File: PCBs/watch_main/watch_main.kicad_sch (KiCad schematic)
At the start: 1 part, among them U101 Watch_Outline

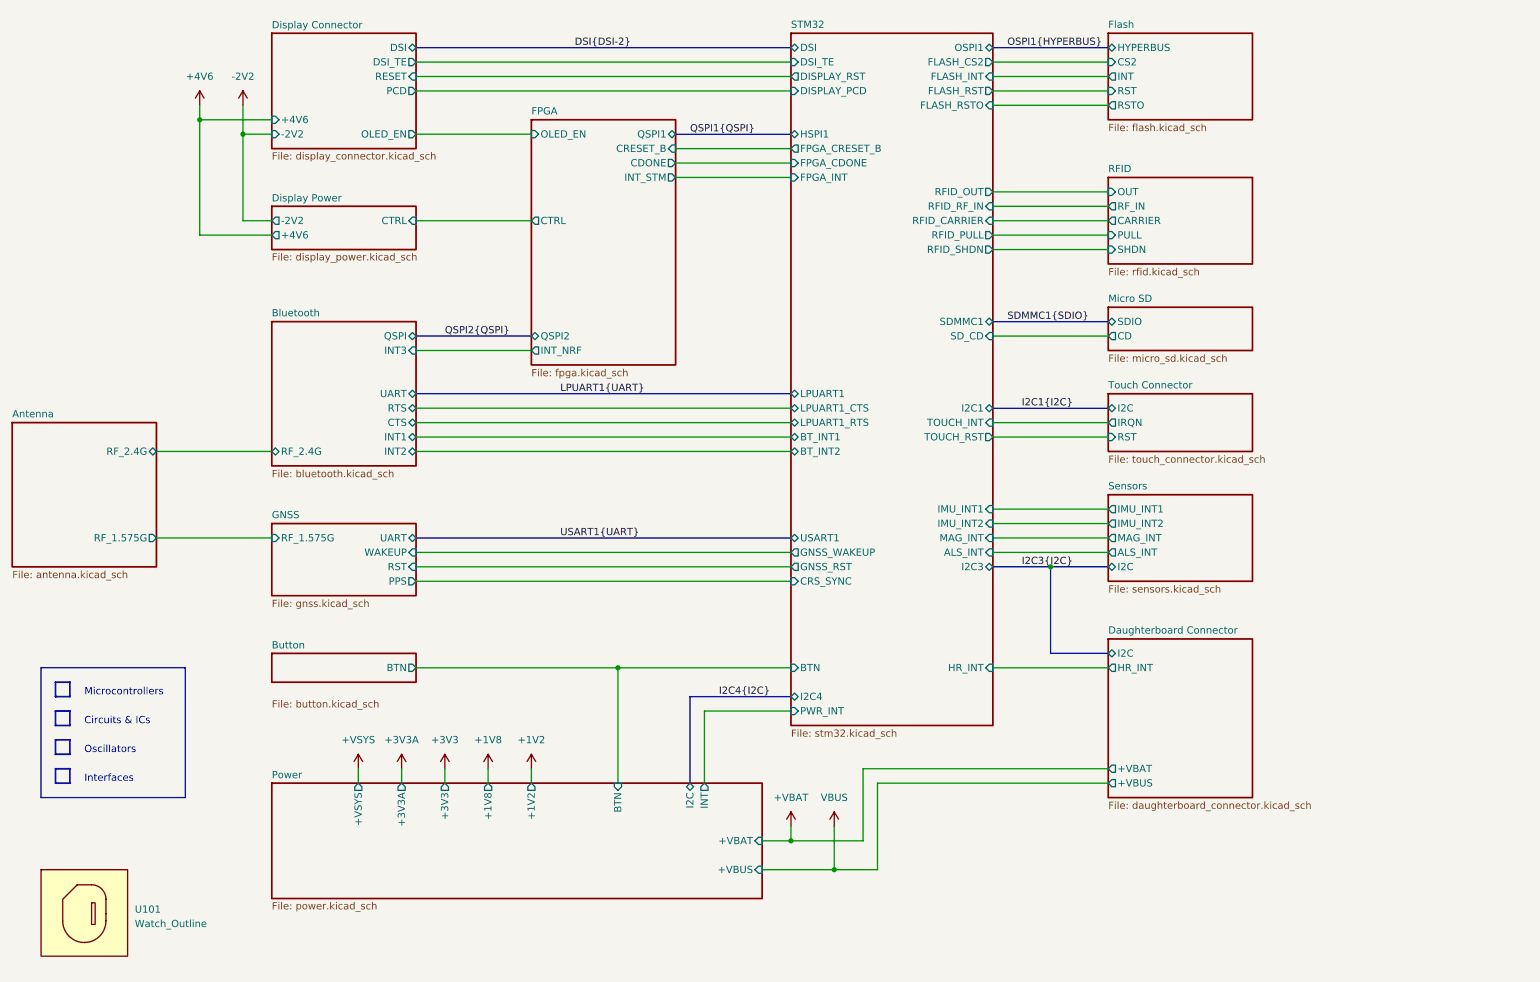
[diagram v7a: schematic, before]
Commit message: Progress with schematic and RFID simulations
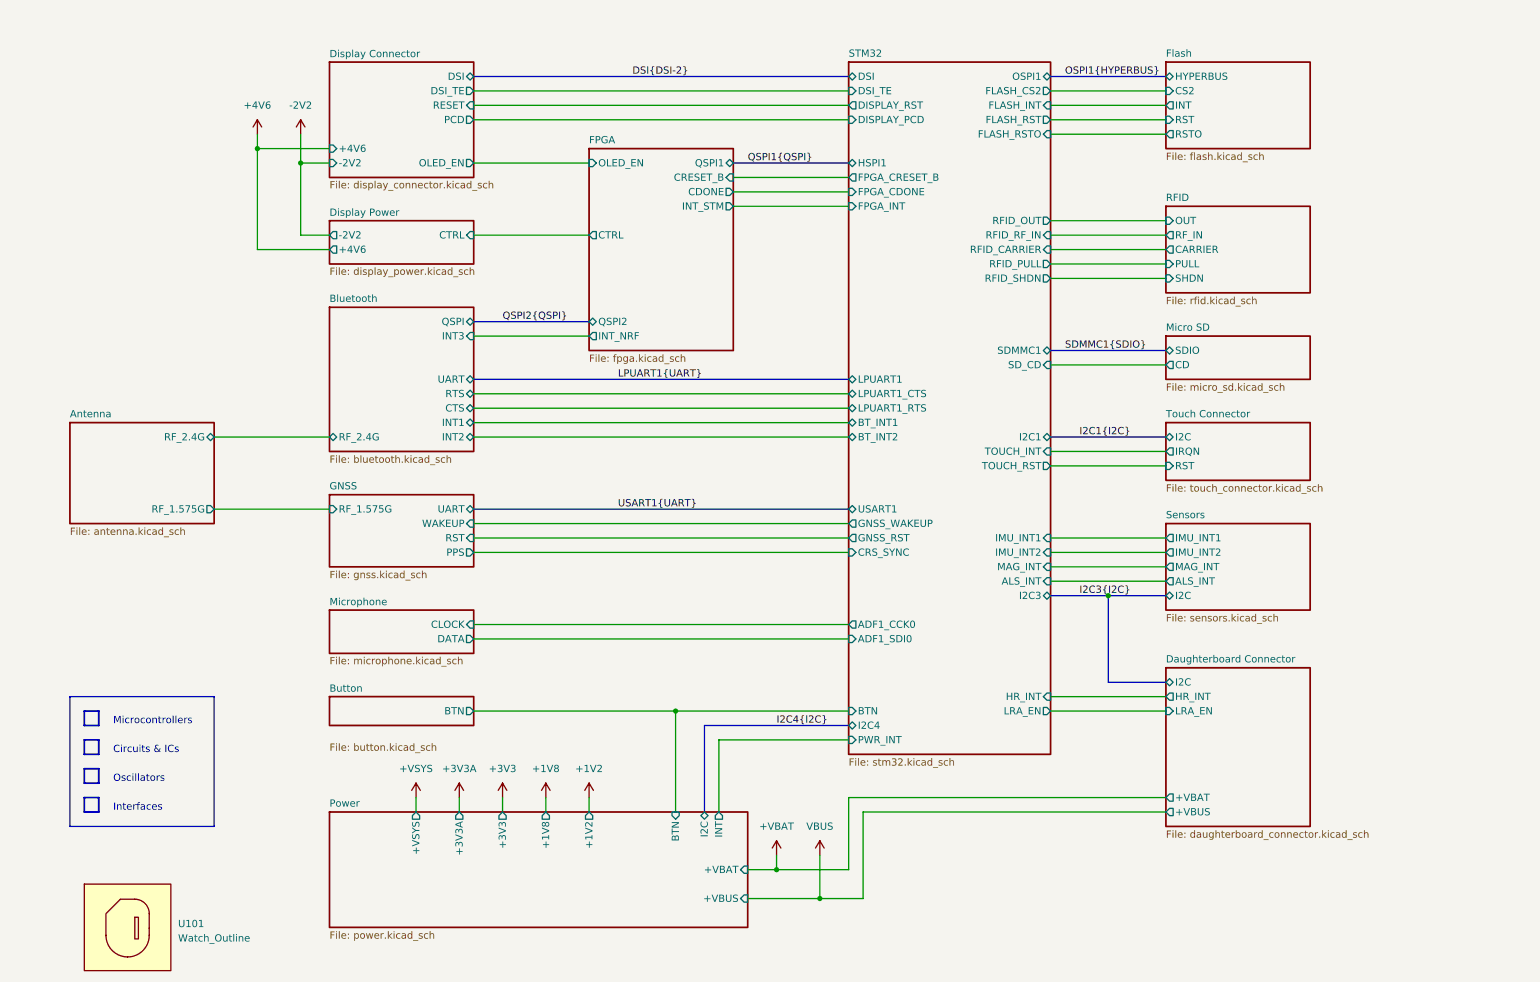
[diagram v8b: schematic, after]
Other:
- added sheet Microphone (microphone.kicad_sch)
- sheet Daughterboard Connector ports: added LRA_EN; removed none
- sheet STM32 ports: added ADF1_CCK0, ADF1_SDI0, LRA_EN; removed none
- moved on the sheet: U101
